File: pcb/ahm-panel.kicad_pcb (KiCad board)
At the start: 2 copper layers, 162 x 82 mm, 81 parts, among them J1 UEXT 2x5 box header, J2 JST XH 2-pin, SW1 6x6 mm tact, 5 mm high, SW2 6x6 mm tact, 5 mm high, SW3 6x6 mm tact, 5 mm high, SW4 6x6 mm tact, 5 mm high, U1 MCP23017-E/SO, U2 74AHCT1G125

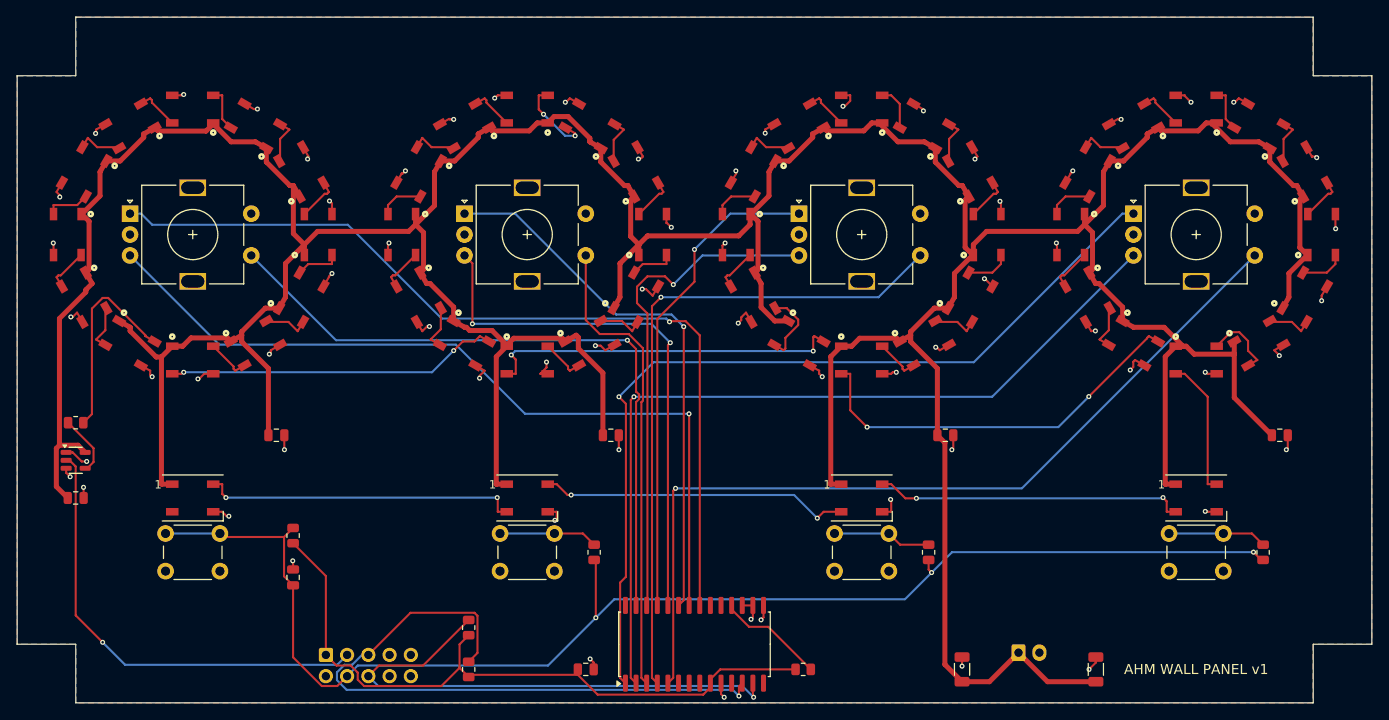
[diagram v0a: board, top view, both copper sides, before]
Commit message: PCB review fixes: scene ladder for the Olimex diode, decoupling, power cap
- The Olimex feeds UEXT pin 4 to GPIO36 through a Schottky diode with its own
  10k pull-up (Rev L schematic). With the board's own pull-up the ladder read
  about 0.4 V too high and DJ/IPAD would be confused. Dropped R1, ladder is now
  0/3.3k/8.2k/22k with PCB-specific thresholds in the firmware.
- Dropped the 4.7k I2C pull-ups (the Olimex has 2.2k).
- MCP23017 decoupling cap moved under VDD/VSS (was 16 mm away); re-routed.
- LED brightness capped at 160 to stay well inside the Olimex 5 V / 2 A rail.

Co-Authored-By: Claude Opus 5.5 (1M context) <noreply@anthropic.com>
Claude-Session: https://claude.ai/code/session_01VPESywWKp5d8Boox5CGCGB
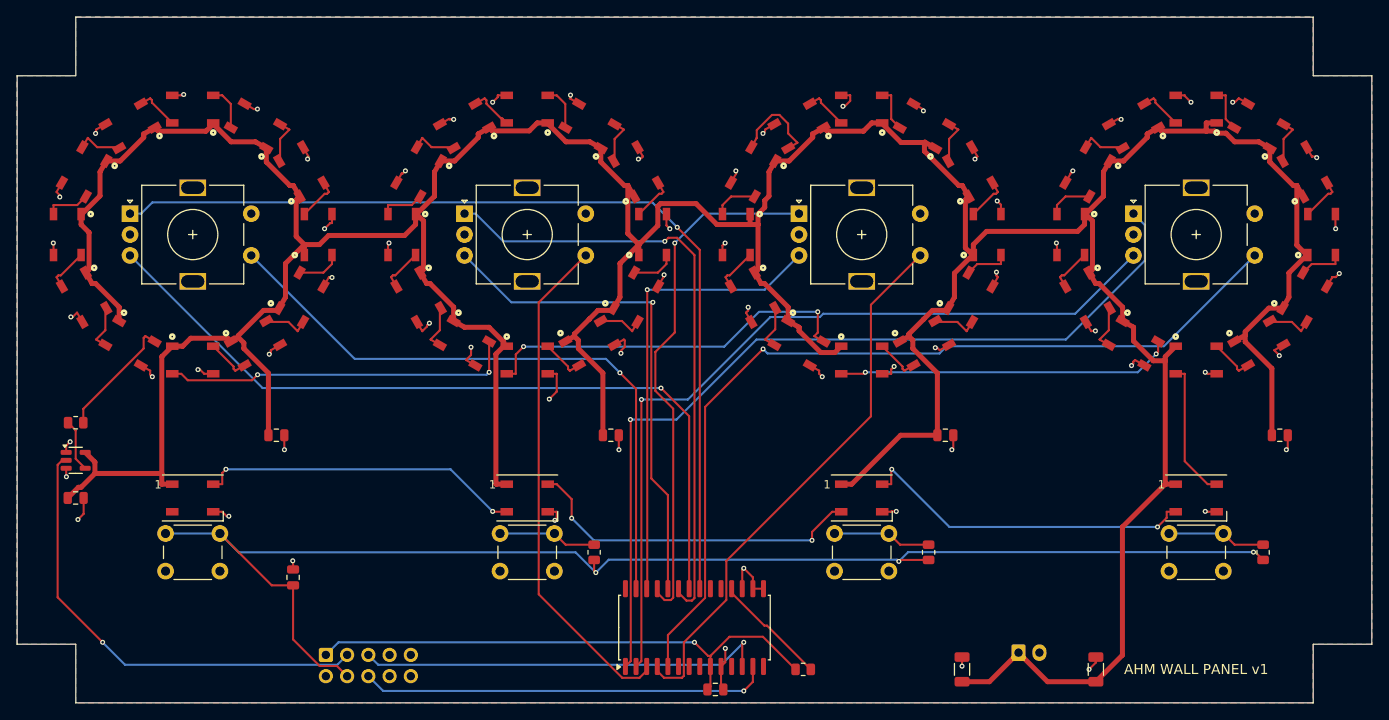
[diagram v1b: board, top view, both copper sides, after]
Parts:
- removed R1: 10k, R_0805_2012Metric
- removed R6, R7: 4.7k, R_0805_2012Metric
- R2: value 2.2k -> 3.3k
- R3: value 4.7k -> 8.2k
- R4: value 10k -> 22k
- moved C2 15.7 mm to (87.5, 84.4)
- moved U1 2.00 mm to (85.0, 77.0)
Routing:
- net SCL: track 77.3 -> 49.5 mm
- net +5V: track 596.3 -> 575.6 mm
- net +3V3: track 82.5 -> 64.2 mm, vias 0 -> 1
- net SDA: track 63.6 -> 49.0 mm
- net ENC3_SW: track 79.9 -> 66.1 mm, vias 1 -> 0
- net LED_DATA: track 24.2 -> 14.7 mm
- net ENC2_A: track 65.4 -> 73.8 mm
- net D36: track 47.8 -> 40.2 mm
- net GND: track 126.4 -> 132.8 mm, vias 66 -> 64
- net D28: track 5.55 -> 11.2 mm
- net ENC1_SW: track 81.6 -> 76.5 mm
- net ENC1_A: track 106.5 -> 111.6 mm
- net D18: track 10.3 -> 5.37 mm, vias 2 -> 0
- net ENC3_B: track 60.4 -> 55.6 mm
- net ENC3_A: track 58.7 -> 63.4 mm
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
